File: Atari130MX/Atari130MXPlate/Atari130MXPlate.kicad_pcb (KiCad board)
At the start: 2 copper layers, 308 x 128.5 mm, 73 parts, among them SW0 SW_Push_45deg, SW1 SW_Push_45deg, SW2 SW_Push_45deg, SW3 SW_Push_45deg, SW4 SW_Push_45deg, SW5 SW_Push_45deg, SW6 SW_Push_45deg, SW7 SW_Push_45deg, SW8 SW_Push_45deg, SW9 SW_Push_45deg

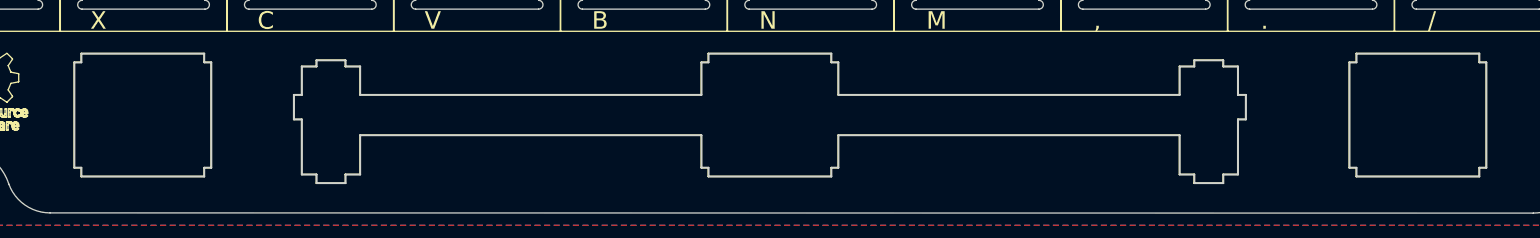
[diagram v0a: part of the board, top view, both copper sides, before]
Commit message: Added extra holes for 6.25U, 9U and stabilizers holes
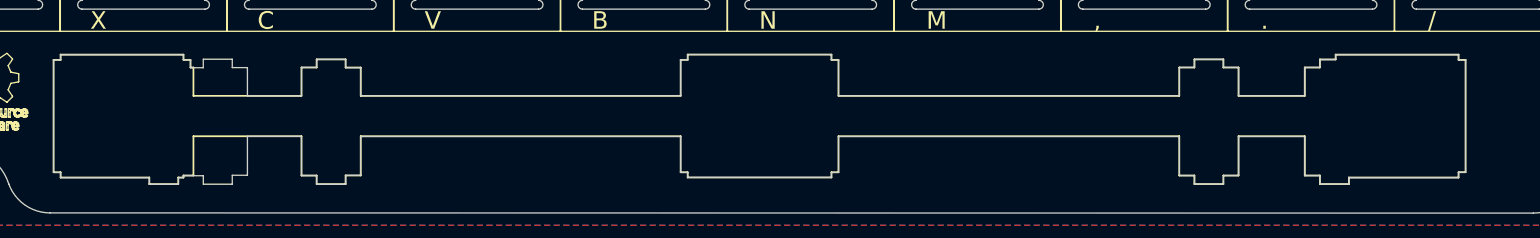
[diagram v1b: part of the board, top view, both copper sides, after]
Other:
- outline, holes or cut-outs redrawn

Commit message: Must be finished. It does not work
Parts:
- added REF**: SW_Hole_Atari_Space, RetroBitLab:SW_Hole_Atari_Space, F.Cu at (186.5, 139.0)
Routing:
- removed copper zone on B.Cu, net (none)
- removed copper zone on F.Cu, net (none)
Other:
- outline, holes or cut-outs redrawn

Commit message: It's simpler to use a (almost) standard 7U spacebar and two 1u extra keys. In that way, the holes needed are only for extra 9U stabilizers. Even the plate gets simpler.
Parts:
- removed REF**: SW_Hole_Atari_Space, RetroBitLab:SW_Hole_Atari_Space
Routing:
- added copper zone on B.Cu, net (none)
- added copper zone on F.Cu, net (none)
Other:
- outline, holes or cut-outs redrawn
- board text added: "130 MX Keyboard Rev. C.6"
- board text added: "9U spacebar 7U spacebar compatibility plus 2 extra 1U keys"
- board text removed: "130 MX Keyboard Rev. C.5"
